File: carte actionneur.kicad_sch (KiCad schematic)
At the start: 60 parts, among them IC1 LMR51460SQDRRRQ1, IC2 LMR51460SQDRRRQ1, J1 Conn_01x08_Pin, J10 Conn_01x08_Pin, J11 Conn_01x04_Pin, J12 Conn_01x09_Pin, J17 Conn_01x04_Pin, J2 Conn_01x02, J3 Conn_01x04_Pin, J5 Conn_01x03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

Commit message: - Added 3 servo pin, for a total of 12 // - Modified pin assignment to connect to proper PWM arduino pins // - Added pull-down resistors to mosfets // - Deleted PWM lidar pin // - Modified inductor components to fit under the arduino
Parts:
- removed J9: Conn_01x01_Pin, Connector_PinHeader_2.54mm:PinHeader_1x01_P2.54mm_Vertical, symbol Connector:Conn_01x01_Pin
- added R1, R2, R3, R4, R5, R6, R7, R8: 1k, Resistor_SMD:R_1206_3216Metric, symbol Device:R_Small
- J12, J7, J8: value Conn_01x09_Pin -> Conn_01x12_Pin; footprint Connector_PinHeader_2.54mm:PinHeader_1x09_P2.54mm_Vertical -> Connector_PinHeader_2.54mm:PinHeader_1x12_P2.54mm_Vertical; symbol Connector:Conn_01x09_Pin -> Connector:Conn_01x12_Pin
- L1, L2: footprint Inductor_SMD:L_Coilcraft_XAL6030-XXX -> HCMA0703-8R2-R:INDPM7168X300N
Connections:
- net +5V: now also J7.10 (Pin_10), J7.11 (Pin_11), J7.12 (Pin_12)
- net GND: now also J8.10 (Pin_10), J8.11 (Pin_11), J8.12 (Pin_12), R1.1, R2.2, R3.1, R4.2, R5.1, R6.2, R7.2, R8.1
- net Mosfet1: now also R1.2
- net Mosfet2: now also R2.1
- net Mosfet3: now also R3.2
- net Mosfet4: now also R4.1
- net Mosfet5: now also U1.D37, R8.2; no longer U1.D36
- net Mosfet6: now also U1.D36, R7.1; no longer U1.D37
- net Mosfet7: now also U1.D39, R5.2; no longer U1.D38
- net Mosfet8: now also U1.D38, R6.1; no longer U1.D39
- net STEP1: now also U1.D44; no longer U1.D2
- net STEP2: now also U1.D45; no longer U1.D3
- net Servo1: now also U1.D2; no longer U1.D10
- net Servo2: now also U1.D3; no longer U1.D13
- net Servo3: now also U1.D4; no longer U1.D12
- net Servo4: now also U1.D5; no longer U1.D15
- net Servo5: now also U1.D6; no longer U1.D14
- net Servo6: now also U1.D7; no longer U1.D17
- net Servo7: now also U1.D9; no longer U1.D16
- net Servo8: now also U1.D8; no longer U1.D19
- net Servo9: now also U1.D11; no longer U1.D18
- net PWM_LIDAR: no longer names the net of U1.D46
- new net Servo10: J12.10 (Pin_10), U1.D10
- new net Servo11: J12.11 (Pin_11), U1.D13
- new net Servo12: J12.12 (Pin_12), U1.D12
- no-connect marks 41 -> 40

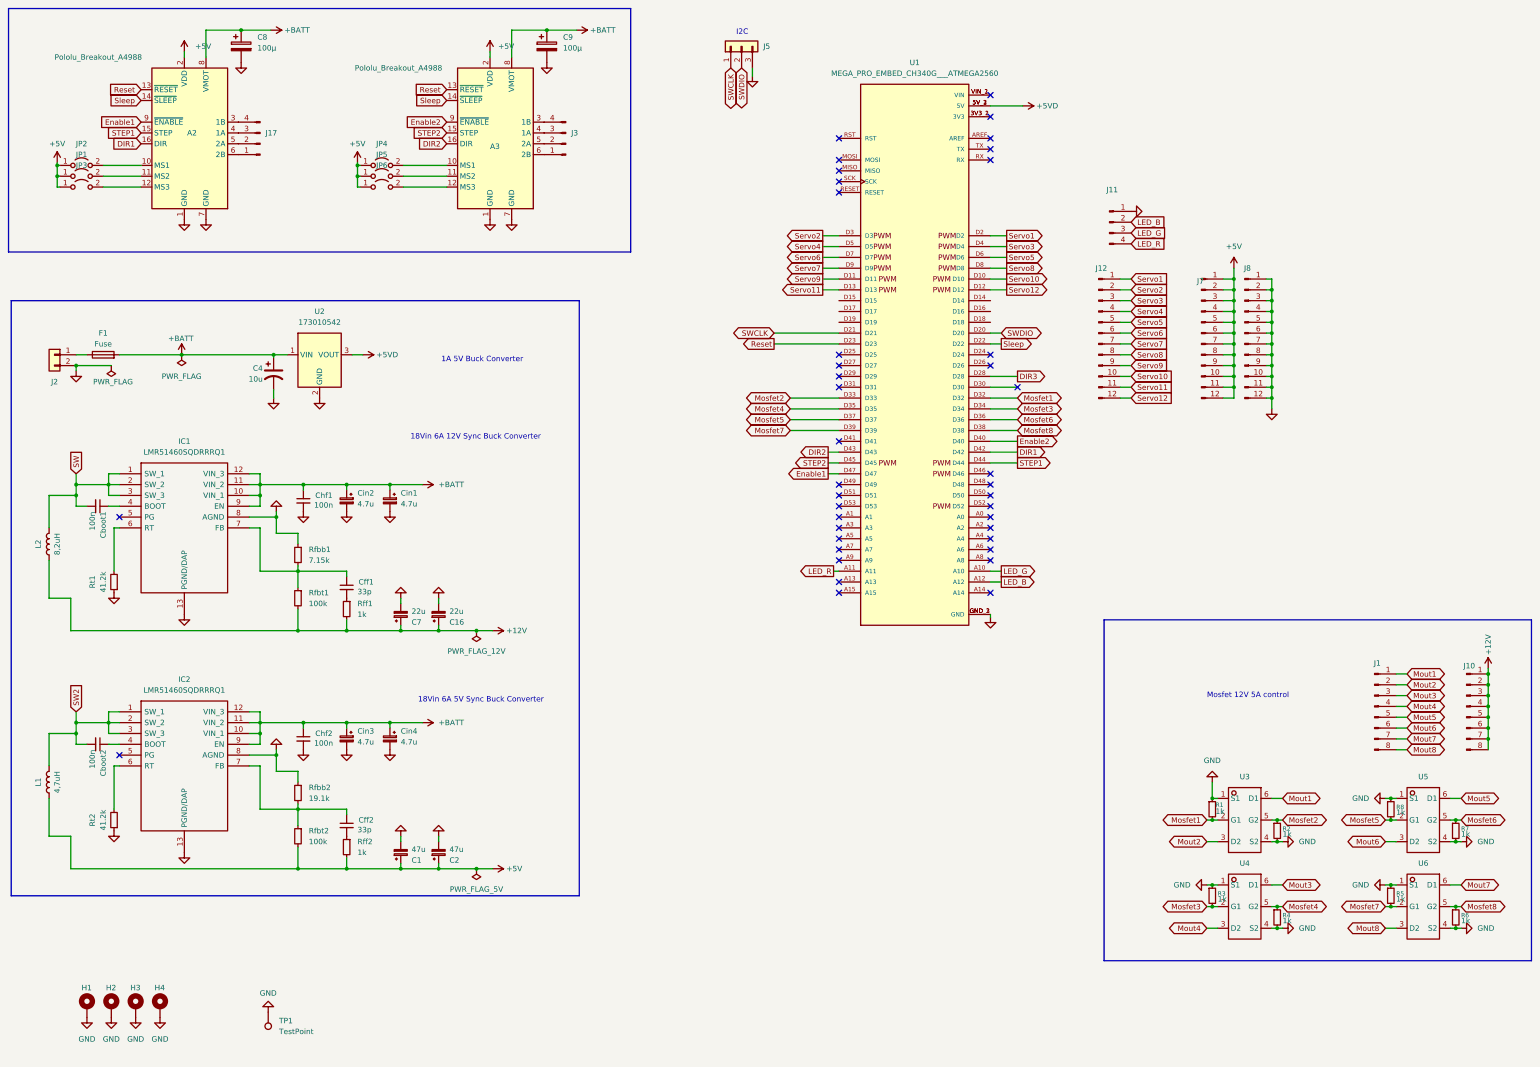
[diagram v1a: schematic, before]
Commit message: Added TCA9548A module for I2C multiplexing
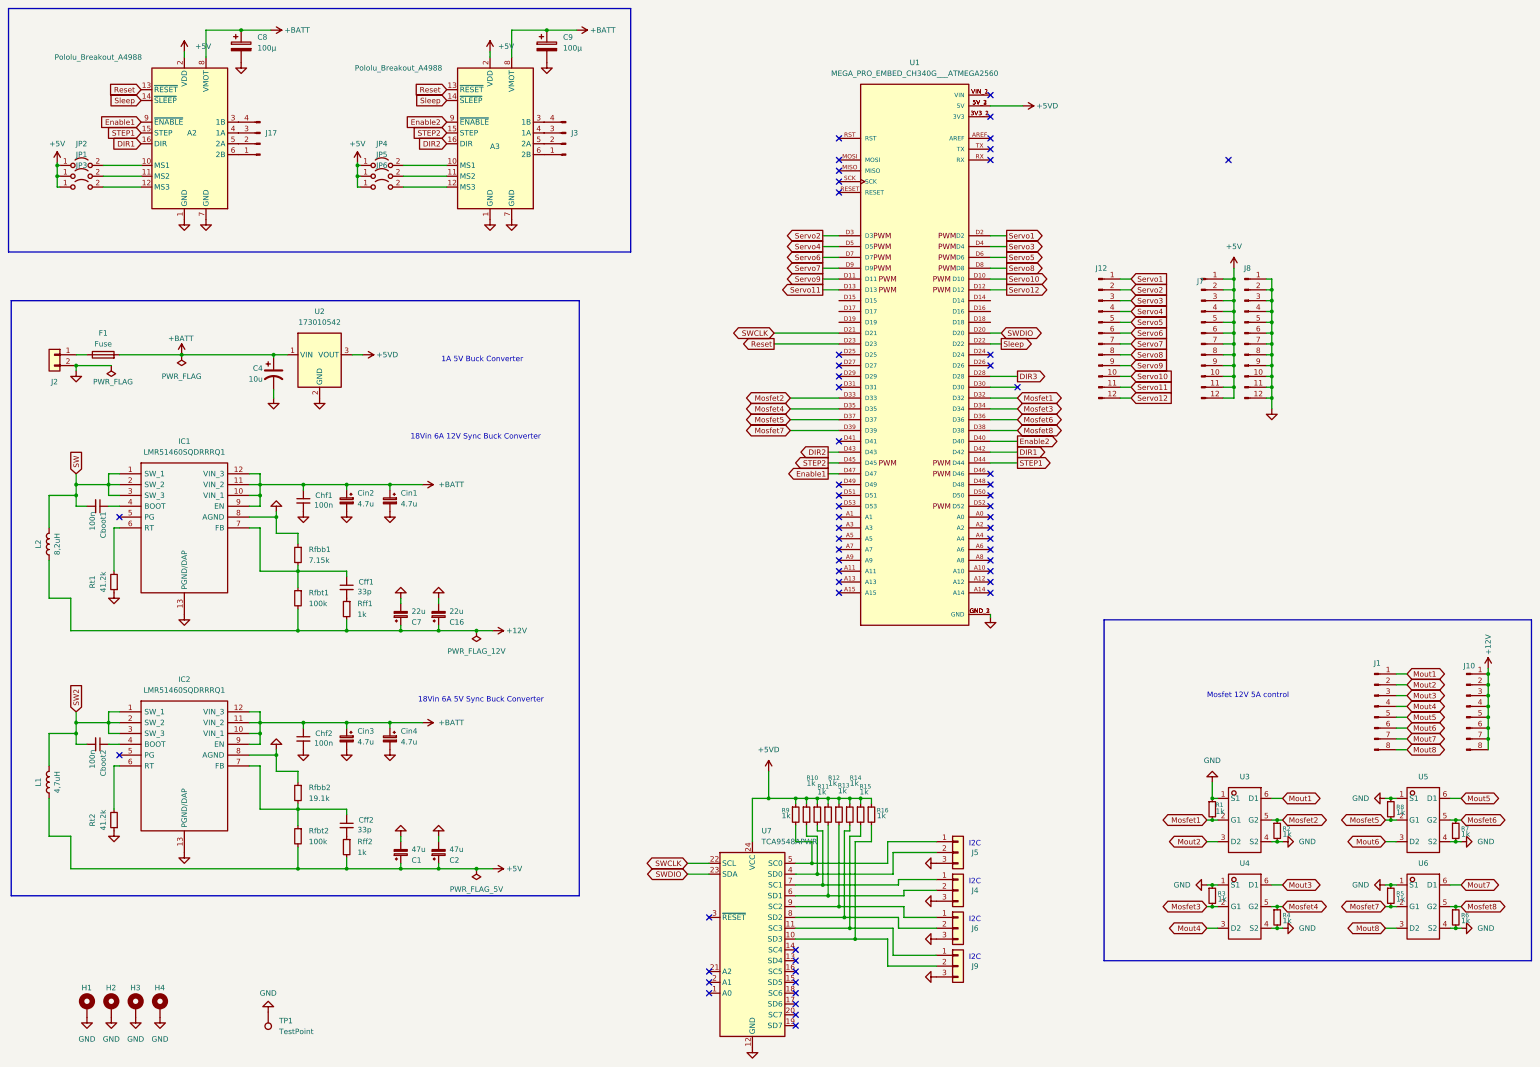
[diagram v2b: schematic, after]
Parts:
- removed J11: Conn_01x04_Pin, Connector_PinHeader_2.54mm:PinHeader_1x04_P2.54mm_Vertical, symbol Connector:Conn_01x04_Pin
- added J4, J6, J9: Conn_01x03, Connector_JST:JST_XH_B3B-XH-A_1x03_P2.50mm_Vertical, symbol Connector_Generic:Conn_01x03
- added R10, R11, R12, R13, R14, R15, R16, R9: 1k, Resistor_SMD:R_1206_3216Metric, symbol Device:R_Small
- added U7: TCA9548APWR, Adafruit TCA9548A:ADA Perso, symbol Interface_Expansion:TCA9548APWR
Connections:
- net +5VD: now also R10.1, R11.1, R12.1, R13.1, R14.1, R15.1, R16.1, R9.1, U7.24 (VCC)
- net GND: now also J4.3 (Pin_3), J6.3 (Pin_3), J9.3 (Pin_3), U7.12 (GND)
- net SWCLK: now also U7.22 (SCL); no longer J5.1 (Pin_1)
- net SWDIO: now also U7.23 (SDA); no longer J5.2 (Pin_2)
- net LED_B: no longer names the net of U1.A12
- net LED_G: no longer names the net of U1.A10
- net LED_R: no longer names the net of U1.A11
- new net: J9.2 (Pin_2), R16.2, U7.10 (SD3)
- new net: J4.1 (Pin_1), R11.2, U7.7 (SC1)
- new net: J9.1 (Pin_1), R15.2, U7.11 (SC3)
- new net: J5.2 (Pin_2), R10.2, U7.4 (SD0)
- new net: J5.1 (Pin_1), R9.2, U7.5 (SC0)
- new net: J4.2 (Pin_2), R12.2, U7.6 (SD1)
- new net: J6.2 (Pin_2), R14.2, U7.8 (SD2)
- new net: J6.1 (Pin_1), R13.2, U7.9 (SC2)
- no-connect marks 40 -> 56
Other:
- moved on the sheet: J5

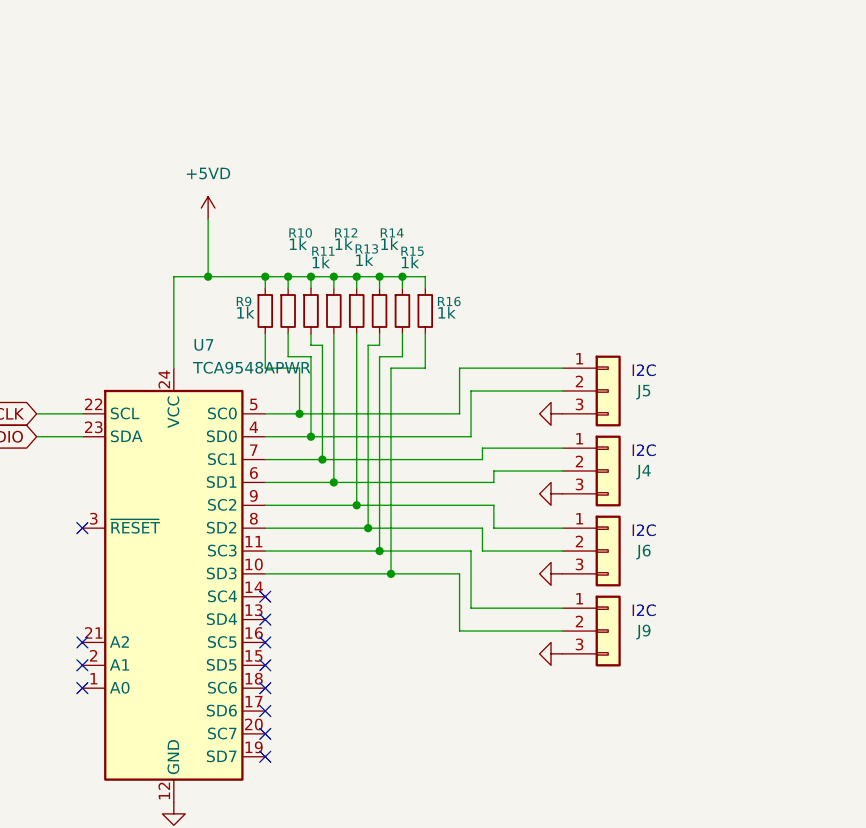
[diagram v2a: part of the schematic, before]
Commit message: Modified pins and added 5V to I2C
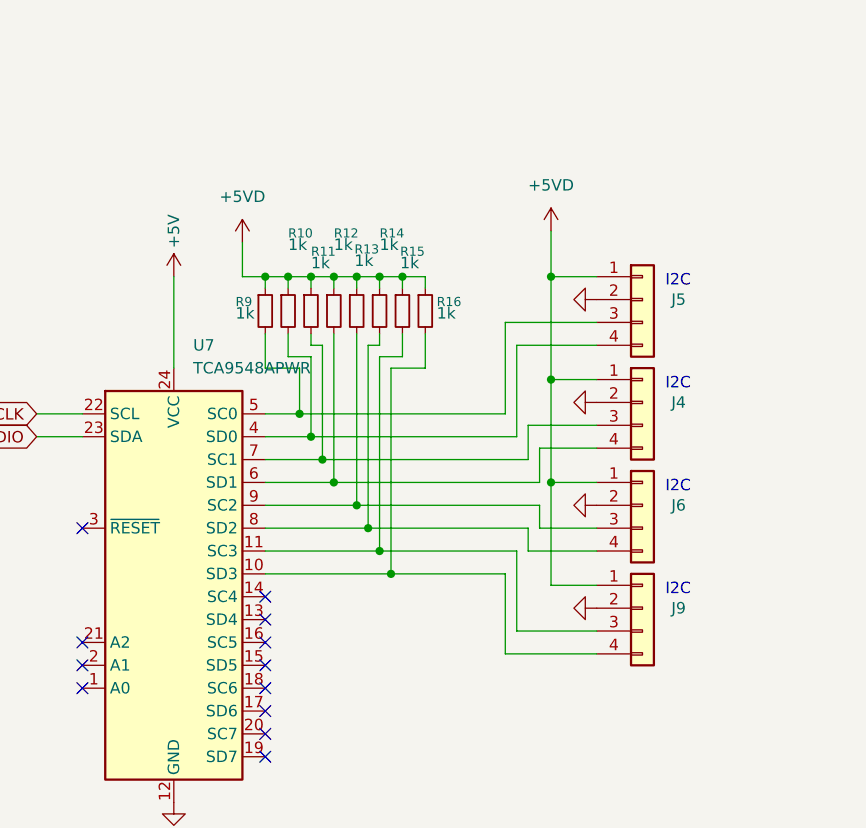
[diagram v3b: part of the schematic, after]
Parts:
- removed J4, J6, J9: Conn_01x03, Connector_JST:JST_XH_B3B-XH-A_1x03_P2.50mm_Vertical, symbol Connector_Generic:Conn_01x03
- added J4, J6, J9: Conn_01x03, Connector_PinHeader_2.54mm:PinHeader_1x04_P2.54mm_Vertical, symbol Connector_Generic:Conn_01x04
- J5: footprint Connector_JST:JST_XH_B3B-XH-A_1x03_P2.50mm_Vertical -> Connector_PinHeader_2.54mm:PinHeader_1x04_P2.54mm_Vertical; symbol Connector_Generic:Conn_01x03 -> Connector_Generic:Conn_01x04
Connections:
- net +5V: now also U7.24 (VCC)
- net +5VD: now also J5.1 (Pin_1), J4.1 (Pin_1), J6.1 (Pin_1), J9.1 (Pin_1); no longer U7.24 (VCC)
- net GND: now also J5.2 (Pin_2), J4.2 (Pin_2), J6.2 (Pin_2), J9.2 (Pin_2); no longer J5.3 (Pin_3)
- net at R16.2, U7.10 (SD3): now also J9.4 (Pin_4)
- net at R11.2, U7.7 (SC1): now also J4.3 (Pin_3)
- net at R15.2, U7.11 (SC3): now also J9.3 (Pin_3)
- net at R10.2, U7.4 (SD0): now also J5.4 (Pin_4); no longer J5.2 (Pin_2)
- net at R9.2, U7.5 (SC0): now also J5.3 (Pin_3); no longer J5.1 (Pin_1)
- net at R12.2, U7.6 (SD1): now also J4.4 (Pin_4)
- net at R14.2, U7.8 (SD2): now also J6.4 (Pin_4)
- net at R13.2, U7.9 (SC2): now also J6.3 (Pin_3)

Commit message: fix warning pcb
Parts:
- U1: footprint lib-arduino:MODULE_MEGA_PRO_EMBED_CH340G___ATMEGA2560 -> lib-arduino:MODULE_MEGA_PRO_2_CONNECTOR; symbol MEGA_PRO_EMBED_CH340G___ATMEGA2560:MEGA_PRO_EMBED_CH340G___ATMEGA2560 -> mega_pro_2_connector:MEGA_PRO_EMBED_CH340G___ATMEGA2560
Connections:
- net +5VD: no longer U1.5V_3 (5V)
- net GND: no longer U1.GND_3 (GND)
- net DIR3: no longer names the net of U1.D28
- no-connect marks 56 -> 50
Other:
- moved on the sheet: A3, C4, C8, H1, H2, H3, H4, J3, JP4, JP5, JP6, TP1

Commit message: Modified fuse holder footprint
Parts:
- F1: footprint FuseHolder:FUSE_0154004.DR -> Fuse:Fuseholder_Cylinder-5x20mm_EATON_H15-V-1_Vertical_Closed
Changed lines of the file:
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@@
 			)
 		)
-		(property "Footprint" "FuseHolder:FUSE_0154004.DR"
+		(property "Footprint" "Fuse:Fuseholder_Cylinder-5x20mm_EATON_H15-V-1_Vertical_Closed"
 			(at 67.31 105.918 90)
 			(effects
